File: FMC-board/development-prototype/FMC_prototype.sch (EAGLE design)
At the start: 64 parts, among them J1 DC_POWER_JACK-PJ-102AH, J2 DC_POWER_JACK-PJ-102AH

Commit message: routed B SPI connector
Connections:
- removed net N$17: B.MISO2+
- removed net N$18: B.MISO2-
- removed net N$19: B.MISO1+
- removed net N$20: B.MISO1-
- removed net N$21: B.MOSI+
- removed net N$22: B.MOSI-
- removed net N$23: B.SCLK+
- removed net N$24: B.SCLK-
- removed net N$25: B.!CS!+
- removed net N$26: B.!CS!-
- new net B_CS+: B.!CS!+, U$4G$1.P$37
- new net B_CS-: B.!CS!-, U$4G$1.P$38
- new net B_MISO1+: B.MISO1+, U$4G$1.P$28
- new net B_MISO1-: B.MISO1-, U$4G$1.P$29
- new net B_MISO2+: B.MISO2+, U$4G$1.P$25
- new net B_MISO2-: B.MISO2-, U$4G$1.P$26
- new net B_MOSI+: B.MOSI+, U$4G$1.P$31
- new net B_MOSI-: B.MOSI-, U$4G$1.P$32
- new net B_SCLK+: B.SCLK+, U$4G$1.P$34
- new net B_SCLK-: B.SCLK-, U$4G$1.P$35
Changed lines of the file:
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@@
-</segment>
-</net>
-<net name="N$17" class="0">
-<segment>
-<pinref part="B" gate="A" pin="MISO2+"/>
-<wire x1="66.04" y1="20.32" x2="71.12" y2="20.32" width="0.1524" layer="91"/>
-<label x="71.12" y="20.32" size="1.778" layer="95"/>
-</segment>
-</net>
-<net name="N$18" class="0">
-<segment>
-<pinref part="B" gate="A" pin="MISO2-"/>
-<wire x1="66.04" y1="22.86" x2="71.12" y2="22.86" width="0.1524" layer="91"/>
-<label x="71.12" y="22.86" size="1.778" layer="95"/>
-</segment>
-</net>
-<net name="N$19" class="0">
-<segment>
-<pinref part="B" gate="A" pin="MISO1+"/>
-<wire x1="66.04" y1="27.94" x2="71.12" y2="27.94" width="0.1524" layer="91"/>
-<label x="71.12" y="27.94" size="1.778" layer="95"/>
-</segment>
-</net>
-<net name="N$20" class="0">
-<segment>
-<pinref part="B" gate="A" pin="MISO1-"/>
-<wire x1="66.04" y1="30.48" x2="71.12" y2="30.48" width="0.1524" layer="91"/>
-<label x="71.12" y="30.48" size="1.778" layer="95"/>
-</segment>
-</net>
-<net name="N$21" class="0">
-<segment>
-<pinref part="B" gate="A" pin="MOSI+"/>
-<wire x1="66.04" y1="35.56" x2="71.12" y2="35.56" width="0.1524" layer="91"/>
-<label x="71.12" y="35.56" size="1.778" layer="95"/>
-</segment>
-</net>
-<net name="N$22" class="0">
-<segment>
-<pinref part="B" gate="A" pin="MOSI-"/>
-<wire x1="66.04" y1="38.1" x2="71.12" y2="38.1" width="0.1524" layer="91"/>
-<label x="71.12" y="38.1" size="1.778" layer="95"/>
-</segment>
-</net>
-<net name="N$23" class="0">
-<segment>
-<pinref part="B" gate="A" pin="SCLK+"/>
-<wire x1="66.04" y1="43.18" x2="71.12" y2="43.18" width="0.1524" layer="91"/>
-<label x="71.12" y="43.18" size="1.778" layer="95"/>
-</segment>
-</net>
-<net name="N$24" class="0">
-<segment>
-<pinref part="B" gate="A" pin="SCLK-"/>
-<wire x1="66.04" y1="45.72" x2="71.12" y2="45.72" width="0.1524" layer="91"/>
-<label x="71.12" y="45.72" size="1.778" layer="95"/>
-</segment>
-</net>
-<net name="N$25" class="0">
-<segment>
-<pinref part="B" gate="A" pin="!CS!+"/>
-<wire x1="66.04" y1="50.8" x2="71.12" y2="50.8" width="0.1524" layer="91"/>
-<label x="71.12" y="50.8" size="1.778" layer="95"/>
-</segment>
-</net>
-<net name="N$26" class="0">
-<segment>
-<pinref part="B" gate="A" pin="!CS!-"/>
-<wire x1="66.04" y1="53.34" x2="71.12" y2="53.34" width="0.1524" layer="91"/>
-<label x="71.12" y="53.34" size="1.778" layer="95"/>
 </segment>
 </net>
@@
 </segment>
 </net>
+<net name="B_MISO2+" class="0">
+<segment>
+<pinref part="U$4" gate="G$1" pin="P$25"/>
+<wire x1="287.02" y1="83.82" x2="266.7" y2="83.82" width="0.1524" layer="91"/>
+<label x="266.7" y="83.82" size="1.778" layer="95" rot="R180"/>
+</segment>
+<segment>
+<pinref part="B" gate="A" pin="MISO2+"/>
+<wire x1="66.04" y1="20.32" x2="71.12" y2="20.32" width="0.1524" layer="91"/>
+<label x="71.12" y="20.32" size="1.778" layer="95"/>
+</segment>
+</net>
+<net name="B_MISO2-" class="0">
+<segment>
+<pinref part="U$4" gate="G$1" pin="P$26"/>
+<wire x1="287.02" y1="81.28" x2="266.7" y2="81.28" width="0.1524" layer="91"/>
+<label x="266.7" y="81.28" size="1.778" layer="95" rot="R180"/>
+</segment>
+<segment>
+<pinref part="B" gate="A" pin="MISO2-"/>
+<wire x1="66.04" y1="22.86" x2="71.12" y2="22.86" width="0.1524" layer="91"/>
+<label x="71.12" y="22.86" size="1.778" layer="95"/>
+</segment>
+</net>
+<net name="B_MISO1+" class="0">
+<segment>
+<pinref part="U$4" gate="G$1" pin="P$28"/>
+<wire x1="287.02" y1="76.2" x2="266.7" y2="76.2" width="0.1524" layer="91"/>
+<label x="266.7" y="76.2" size="1.778" layer="95" rot="R180"/>
+</segment>
+<segment>
+<pinref part="B" gate="A" pin="MISO1+"/>
+<wire x1="66.04" y1="27.94" x2="71.12" y2="27.94" width="0.1524" layer="91"/>
+<label x="71.12" y="27.94" size="1.778" layer="95"/>
+</segment>
+</net>
+<net name="B_MISO1-" class="0">
+<segment>
+<pinref part="U$4" gate="G$1" pin="P$29"/>
+<wire x1="287.02" y1="73.66" x2="266.7" y2="73.66" width="0.1524" layer="91"/>
+<label x="266.7" y="73.66" size="1.778" layer="95" rot="R180"/>
+</segment>
+<segment>
+<pinref part="B" gate="A" pin="MISO1-"/>
+<wire x1="66.04" y1="30.48" x2="71.12" y2="30.48" width="0.1524" layer="91"/>
+<label x="71.12" y="30.48" size="1.778" layer="95"/>
+</segment>
+</net>
+<net name="B_MOSI+" class="0">
+<segment>
+<pinref part="U$4" gate="G$1" pin="P$31"/>
+<wire x1="287.02" y1="68.58" x2="266.7" y2="68.58" width="0.1524" layer="91"/>
+<label x="266.7" y="68.58" size="1.778" layer="95" rot="R180"/>
+</segment>
+<segment>
+<pinref part="B" gate="A" pin="MOSI+"/>
+<wire x1="66.04" y1="35.56" x2="71.12" y2="35.56" width="0.1524" layer="91"/>
+<label x="71.12" y="35.56" size="1.778" layer="95"/>
+</segment>
+</net>
+<net name="B_MOSI-" class="0">
+<segment>
+<pinref part="U$4" gate="G$1" pin="P$32"/>
+<wire x1="287.02" y1="66.04" x2="266.7" y2="66.04" width="0.1524" layer="91"/>
+<label x="266.7" y="66.04" size="1.778" layer="95" rot="R180"/>
+</segment>
+<segment>
+<pinref part="B" gate="A" pin="MOSI-"/>
+<wire x1="66.04" y1="38.1" x2="71.12" y2="38.1" width="0.1524" layer="91"/>
+<label x="71.12" y="38.1" size="1.778" layer="95"/>
+</segment>
+</net>
+<net name="B_SCLK+" class="0">
+<segment>
+<pinref part="U$4" gate="G$1" pin="P$34"/>
+<wire x1="287.02" y1="60.96" x2="266.7" y2="60.96" width="0.1524" layer="91"/>
+<label x="266.7" y="60.96" size="1.778" layer="95" rot="R180"/>
+</segment>
+<segment>
+<pinref part="B" gate="A" pin="SCLK+"/>
+<wire x1="66.04" y1="43.18" x2="71.12" y2="43.18" width="0.1524" layer="91"/>
+<label x="71.12" y="43.18" size="1.778" layer="95"/>
+</segment>
+</net>
+<net name="B_SCLK-" class="0">
+<segment>
+<pinref part="U$4" gate="G$1" pin="P$35"/>
+<wire x1="287.02" y1="58.42" x2="266.7" y2="58.42" width="0.1524" layer="91"/>
+<label x="266.7" y="58.42" size="1.778" layer="95" rot="R180"/>
+</segment>
+<segment>
+<pinref part="B" gate="A" pin="SCLK-"/>
+<wire x1="66.04" y1="45.72" x2="71.12" y2="45.72" width="0.1524" layer="91"/>
+<label x="71.12" y="45.72" size="1.778" layer="95"/>
+</segment>
+</net>
+<net name="B_CS+" class="0">
+<segment>
+<pinref part="U$4" gate="G$1" pin="P$37"/>
+<wire x1="287.02" y1="53.34" x2="266.7" y2="53.34" width="0.1524" layer="91"/>
+<label x="266.7" y="53.34" size="1.778" layer="95" rot="R180"/>
+</segment>
+<segment>
+<pinref part="B" gate="A" pin="!CS!+"/>
+<wire x1="66.04" y1="50.8" x2="71.12" y2="50.8" width="0.1524" layer="91"/>
+<label x="71.12" y="50.8" size="1.778" layer="95"/>
+</segment>
+</net>
+<net name="B_CS-" class="0">
+<segment>
+<pinref part="U$4" gate="G$1" pin="P$38"/>
+<wire x1="287.02" y1="50.8" x2="266.7" y2="50.8" width="0.1524" layer="91"/>
+<label x="266.7" y="50.8" size="1.778" layer="95" rot="R180"/>
+</segment>
+<segment>
+<pinref part="B" gate="A" pin="!CS!-"/>
+<wire x1="66.04" y1="53.34" x2="71.12" y2="53.34" width="0.1524" layer="91"/>
+<label x="71.12" y="53.34" size="1.778" layer="95"/>
+</segment>
+</net>

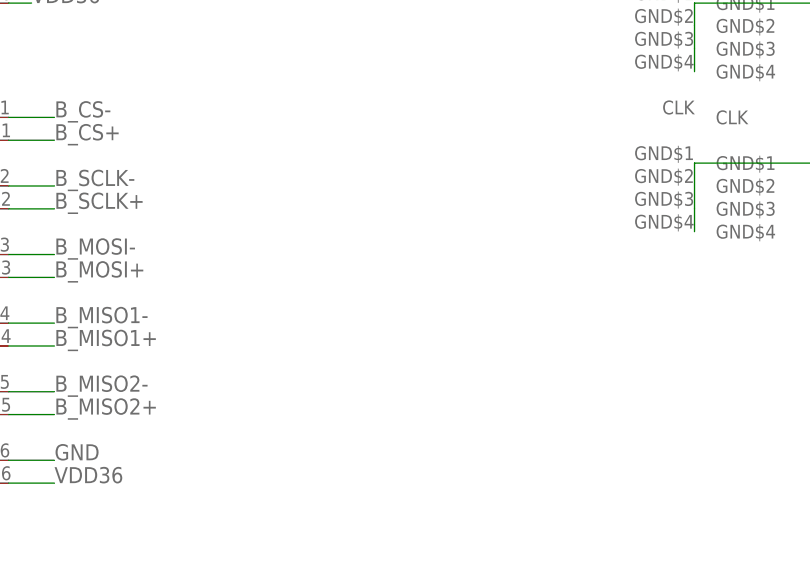
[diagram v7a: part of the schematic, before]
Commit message: added measurement points (just+) to all B connector LVDS signals
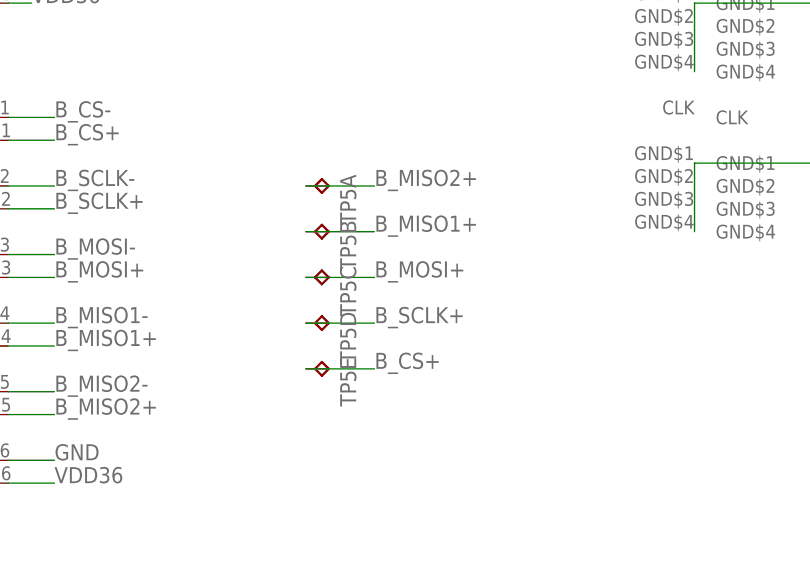
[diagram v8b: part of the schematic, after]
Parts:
- added TP5: TP5P5-25-13, testpad:TP5P5-25-13
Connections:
- net B_CS+: now also TP5E.TP
- net B_MISO1+: now also TP5B.TP
- net B_MISO2+: now also TP5A.TP
- net B_MOSI+: now also TP5C.TP
- net B_SCLK+: now also TP5D.TP
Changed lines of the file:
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@@
 <part name="C23" library="RHD2000_eval_board" deviceset="C" device="_0603" value="10n"/>
 <part name="GND22" library="supply1" deviceset="GND" device=""/>
+<part name="TP5" library="testpad" deviceset="TP5" device="P5-25-13"/>
 </parts>
 <sheets>
@@
 <instance part="C23" gate="C" x="144.78" y="-38.1"/>
 <instance part="GND22" gate="1" x="172.72" y="-45.72" rot="R90"/>
+<instance part="TP5" gate="A" x="101.6" y="45.72" rot="R270"/>
+<instance part="TP5" gate="B" x="101.6" y="40.64" rot="R270"/>
+<instance part="TP5" gate="C" x="101.6" y="35.56" rot="R270"/>
+<instance part="TP5" gate="D" x="101.6" y="30.48" rot="R270"/>
+<instance part="TP5" gate="E" x="101.6" y="25.4" rot="R270"/>
 </instances>
 <busses>
@@
 <label x="71.12" y="20.32" size="1.778" layer="95"/>
 </segment>
+<segment>
+<wire x1="99.06" y1="45.72" x2="106.68" y2="45.72" width="0.1524" layer="91"/>
+<label x="106.68" y="45.72" size="1.778" layer="95"/>
+<pinref part="TP5" gate="A" pin="TP"/>
+</segment>
 </net>
 <net name="B_MISO2-" class="0">
@@
 <label x="71.12" y="27.94" size="1.778" layer="95"/>
 </segment>
+<segment>
+<wire x1="99.06" y1="40.64" x2="106.68" y2="40.64" width="0.1524" layer="91"/>
+<label x="106.68" y="40.64" size="1.778" layer="95"/>
+<pinref part="TP5" gate="B" pin="TP"/>
+</segment>
 </net>
 <net name="B_MISO1-" class="0">
@@
 <label x="71.12" y="35.56" size="1.778" layer="95"/>
 </segment>
+<segment>
+<wire x1="99.06" y1="35.56" x2="106.68" y2="35.56" width="0.1524" layer="91"/>
+<label x="106.68" y="35.56" size="1.778" layer="95"/>
+<pinref part="TP5" gate="C" pin="TP"/>
+</segment>
 </net>
 <net name="B_MOSI-" class="0">
@@
 <label x="71.12" y="43.18" size="1.778" layer="95"/>
 </segment>
+<segment>
+<wire x1="99.06" y1="30.48" x2="106.68" y2="30.48" width="0.1524" layer="91"/>
+<label x="106.68" y="30.48" size="1.778" layer="95"/>
+<pinref part="TP5" gate="D" pin="TP"/>
+</segment>
 </net>
 <net name="B_SCLK-" class="0">
@@
 <label x="71.12" y="50.8" size="1.778" layer="95"/>
 </segment>
-</net>
+<segment>
+<wire x1="99.06" y1="25.4" x2="106.68" y2="25.4" width="0.1524" layer="91"/>
+<label x="106.68" y="25.4" size="1.778" layer="95"/>
+<pinref part="TP5" gate="E" pin="TP"/>
+</segment>
+</net>
